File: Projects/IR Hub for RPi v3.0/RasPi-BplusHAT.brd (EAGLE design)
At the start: 65 x 56 mm, 42 parts, among them SW1 SPST_TACT-KMR2, SW2 SPST_TACT-KMR2, SW3 SPST_TACT-KMR2, T1 2N4401, T2 2N4401, T3 2N4401, T4 2N4401, T5 2N4401, U1 CLVC1G32MDCKREPG4

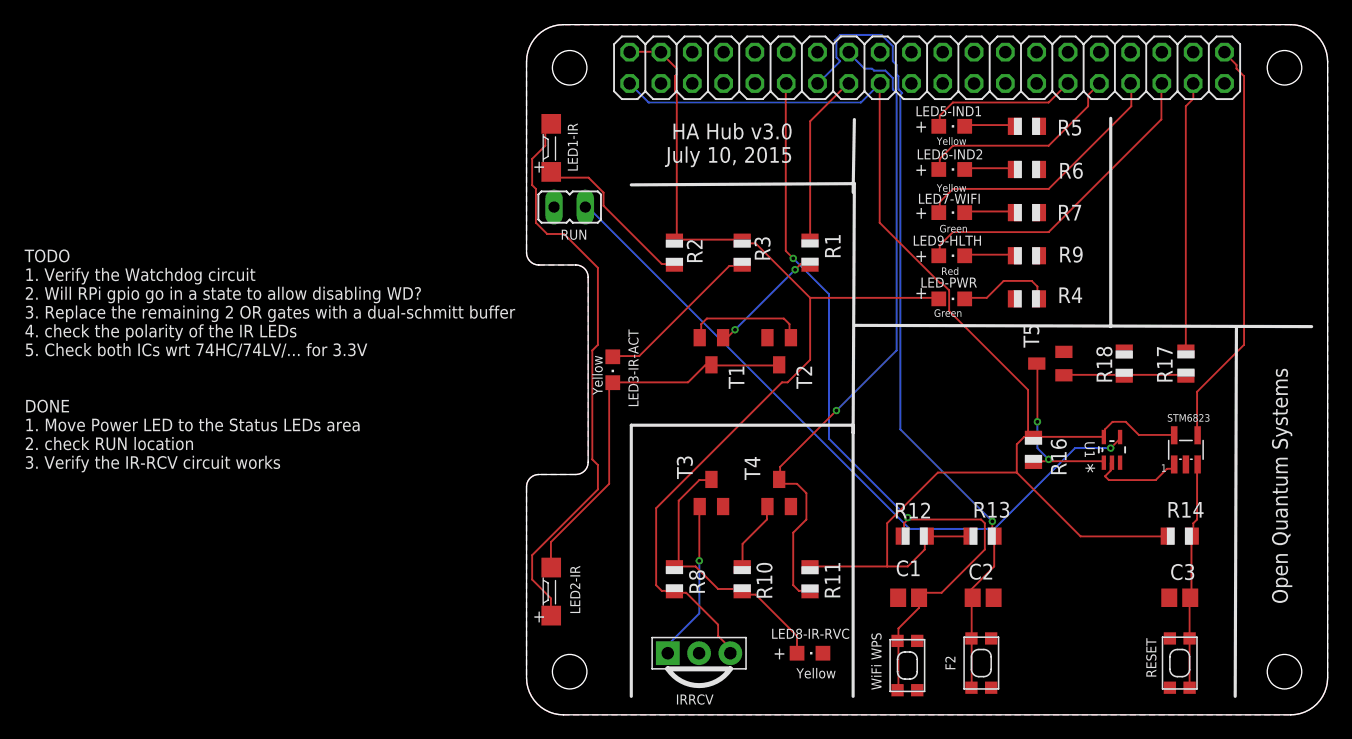
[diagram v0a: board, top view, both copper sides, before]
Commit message: removed Watchdog
... as there is a hardware watchdog on Raspberry Pi, and a good
watchdog daemon  framework for health monitoring
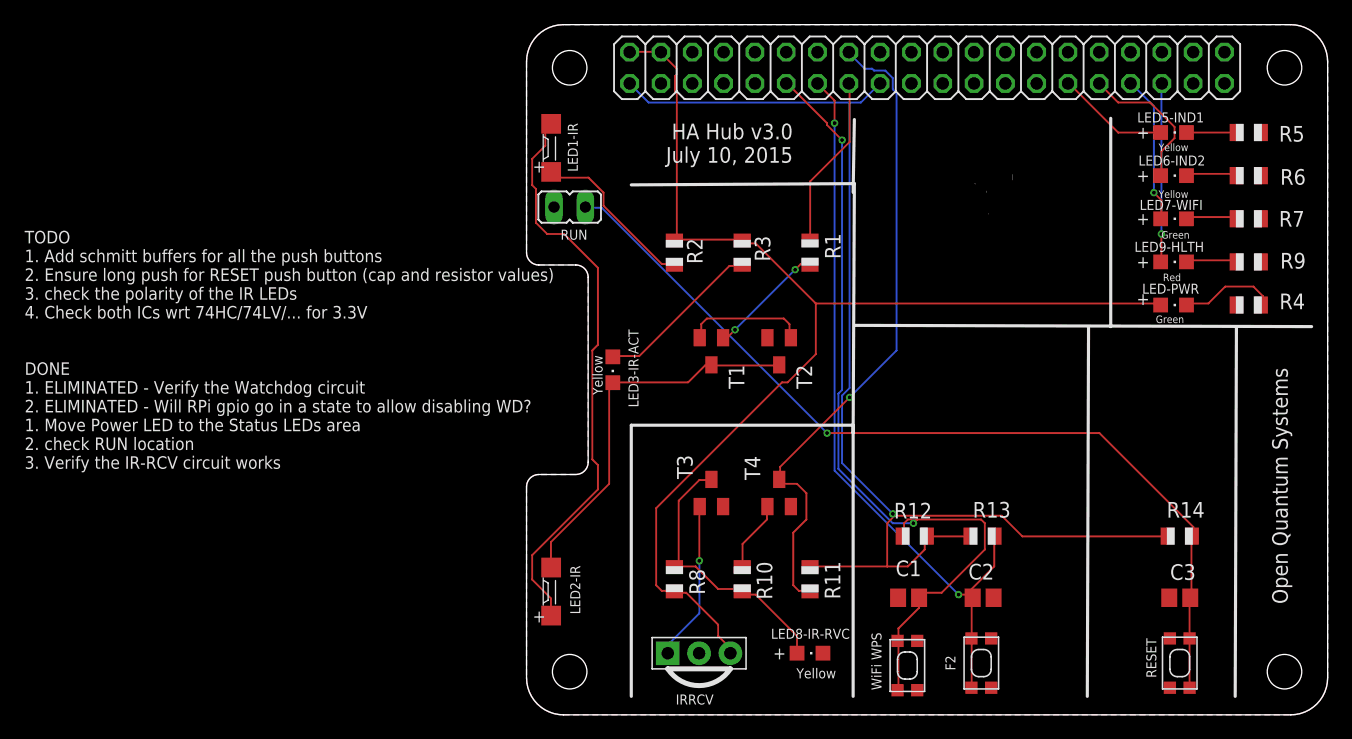
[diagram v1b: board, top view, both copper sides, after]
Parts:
- removed R16, R17, R18: 1K, adafruit:R0805
- removed STM6823: STM6823STM6823, varshneya:SOT-23-5
- removed T5: 2N4401, transistor-neu-to92:SOT23-BEC
- removed U1: CLVC1G32MDCKREPG4, Texas Instruments_By_element14_Batch_1:SOT65P210X110-5N
- moved LED-PWR 18.0 mm to (52.5, 33.2)
- moved LED5-IND1 18.0 mm to (52.5, 47.2)
- moved LED6-IND2 18.0 mm to (52.5, 43.8)
- moved LED7-WIFI 18.0 mm to (52.5, 40.2)
- moved LED9-HLTH 18.0 mm to (52.5, 36.8)
- moved R4 18.0 mm to (58.6, 33.2)
- moved R5 18.0 mm to (58.6, 47.2)
- moved R6 18.0 mm to (58.6, 43.8)
- moved R7 18.0 mm to (58.6, 40.2)
- moved R9 18.0 mm to (58.6, 36.8)
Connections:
- removed net N$12: C3.1, R14.1, STM6823.3, SW3.2, SW3.4
- removed net N$15: R16.2, T5.C, U1.1
- removed net N$20: R17.2, R18.1, T5.B
- removed net N$9: STM6823.1, U1.2
- net +3V3: no longer R16.1, STM6823.5, U1.5
- net GND: no longer R18.2, STM6823.2, T5.E, U1.3
- net GPIO21: no longer STM6823.4
- net GPIO26: no longer R17.1
- net RST: now also C3.1, R14.1, SW3.2, SW3.4; no longer U1.4
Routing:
- net GPIO21: track 33.3 -> 0.00 mm
- net GPIO26: track 22.0 -> 0.00 mm
- net N$12: track 18.4 -> 0.00 mm
- net +3V3: track 117.2 -> 98.9 mm, vias 0 -> 1
- net +5V: track 80.0 -> 97.9 mm
- net RST: track 57.5 -> 73.2 mm
- net N$15: track 14.2 -> 0.00 mm, vias 2 -> 0
- net GPIO19: track 26.0 -> 14.5 mm, vias 0 -> 1
- net N$20: track 10.1 -> 0.00 mm
- net GPIO13: track 21.5 -> 12.0 mm, vias 0 -> 1
- net N$9: track 7.78 -> 0.00 mm
- net GPIO27: track 66.3 -> 60.7 mm, vias 1 -> 2
- net GPIO06: track 16.9 -> 12.0 mm
- net GPIO05: track 12.4 -> 9.16 mm
- net GPIO17: track 64.8 -> 67.0 mm
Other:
- board text added: "TODO 1. Add schmitt buffers for all the push buttons 2. Ensure long push for RESET push button (cap and resistor values) 3. check the polarity of the IR LEDs 4. Check both ICs wrt 74HC/74LV/... for 3.3V DONE 1. ELIMINATED - Verify the Watchdog circuit 2. ELIMINATED - Will RPi gpio go in a state to allow disabling WD? 1. Move Power LED to the Status LEDs area 2. check RUN location 3. Verify the IR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"
- board text removed: "TODO 1. Verify the Watchdog circuit 2. Will RPi gpio go in a state to allow disabling WD? 3. Replace the remaining 2 OR gates with a dual-schmitt buffer 4. check the polarity of the IR LEDs 5. Check both ICs wrt 74HC/74LV/... for 3.3V DONE 1. Move Power LED to the Status LEDs area 2. check RUN location 3. Verify the IR-RCV circuit works"

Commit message: Cleaned up the board layout
... with name and blog URL added; added a smoothening aspect in the
circuit for the RESET push button.
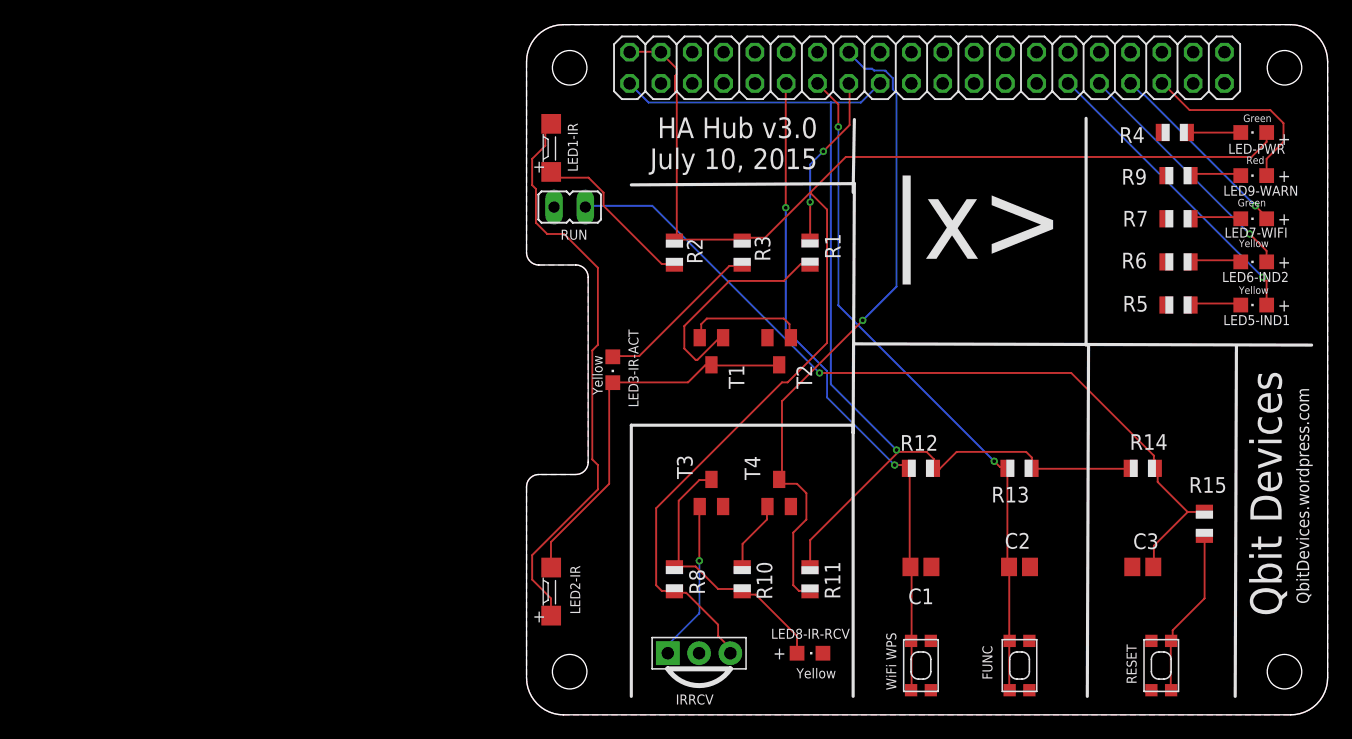
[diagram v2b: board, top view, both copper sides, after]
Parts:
- removed LED9-HLTH: Red, led:CHIPLED_0805
- added LED9-WARN: Red, led:CHIPLED_0805
- added R15: 100K, adafruit:R0805
- R14: value 10K -> 1M
- moved LED-PWR 15.4 mm to (59.0, 47.2), turned to 90 degrees
- moved LED5-IND1 15.4 mm to (59.0, 33.2), turned to 90 degrees
- moved R4 15.2 mm to (52.6, 47.2)
- moved R5 15.1 mm to (52.9, 33.2), turned to 0 degrees
- moved LED6-IND2 9.55 mm to (59.0, 36.8), turned to 90 degrees
- moved R6 9.03 mm to (52.9, 36.8), turned to 0 degrees
- moved R9 9.03 mm to (52.9, 43.8), turned to 0 degrees
- moved LED7-WIFI 6.50 mm to (59.0, 40.2), turned to 90 degrees
- moved R13 6.26 mm to (40.0, 20.0), turned to 0 degrees
- moved R14 6.26 mm to (50.0, 20.0)
- moved R7 5.70 mm to (52.9, 40.2), turned to 0 degrees
- moved R12 5.52 mm to (32.0, 20.0)
- moved C3 3.91 mm to (50.0, 12.0)
- moved C2 3.87 mm to (40.0, 12.0)
- moved SW2 3.11 mm to (40.0, 4.00)
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- renumbered LED8-IR-RVC to LED8-IR-RCV
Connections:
- new net N$1: R15.2, SW3.2, SW3.4
- net GPIO19: now also LED9-WARN.A; no longer LED9-HLTH.A
- net N$16: now also LED9-WARN.C; no longer LED9-HLTH.C
- net RST: now also R15.1; no longer SW3.2, SW3.4
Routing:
- net +5V: track 97.9 -> 118.3 mm
- net GPIO05: track 9.16 -> 24.7 mm, vias 0 -> 1
- net N$1: track 0.00 -> 13.6 mm
- net GPIO17: track 67.0 -> 54.1 mm
- net +3V3: track 98.9 -> 86.1 mm
- net N$5: track 9.54 -> 18.4 mm, vias 2 -> 0
- net GPIO06: track 12.0 -> 20.1 mm, vias 0 -> 1
- net RST: track 73.2 -> 67.3 mm
- net GPIO27: track 60.7 -> 56.0 mm
- net GPIO13: track 12.0 -> 15.7 mm
- net N$21: track 7.94 -> 4.35 mm
- net GPIO19: track 14.5 -> 16.0 mm, vias 1 -> 0
- net GPIO22: vias 0 -> 2
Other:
- board text added: "FUNC"
- board text added: "Home Automation Hub v3.0"
- board text added: "Qbit Devices"
- board text added: "QbitDevices.wordpress.com"
- board text added: "TODO 1. Add schmitt buffers for all the push buttons 2. check the polarity of the IR LEDs 3. Check both ICs wrt 74HC/74LV/... for 3.3V DONE 1. ELIMINATED - Verify the Watchdog circuit 2. ELIMINATED - Will RPi gpio go in a state to allow disabling WD? 3. Ensure long push for RESET push button (cap and resistor values) 4. Move Power LED to the Status LEDs area 5. check RUN location 6. Verify the IR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"
- board text added: "|x>"
- board text removed: "C:/Users/RenuAtul/Desktop/two_slits.bmp"
- board text removed: "F2"
- board text removed: "Open Quantum Systems"
- board text removed: "TODO 1. Add schmitt buffers for all the push buttons 2. Ensure long push for RESET push button (cap and resistor values) 3. check the polarity of the IR LEDs 4. Check both ICs wrt 74HC/74LV/... for 3.3V DONE 1. ELIMINATED - Verify the Watchdog circuit 2. ELIMINATED - Will RPi gpio go in a state to allow disabling WD? 1. Move Power LED to the Status LEDs area 2. check RUN location 3. Verify the IR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"
